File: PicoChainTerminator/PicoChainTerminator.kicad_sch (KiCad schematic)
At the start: 10 parts, among them J1 RJ45, U1 LM78M05_TO252

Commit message: Updated to 1.2
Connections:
- net at R1.1, R2.1: now also J1.6; no longer J1.4
- net at R4.2, R6.1: now also J1.4; no longer J1.6
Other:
- moved on the sheet: R1, R2, R3, R4, R5, R6

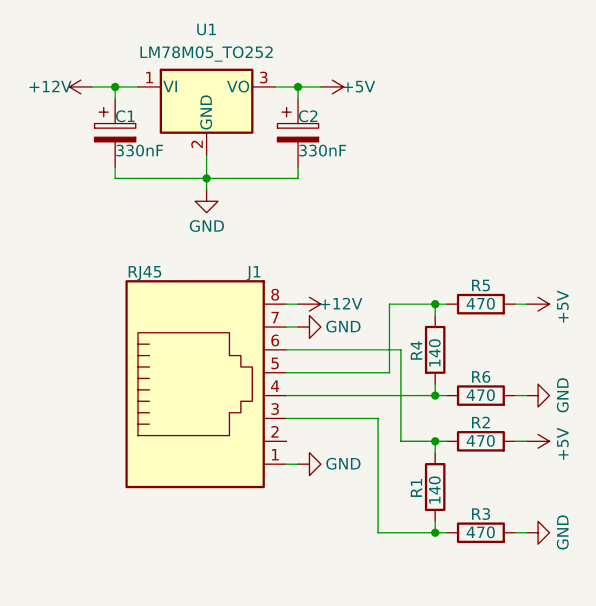
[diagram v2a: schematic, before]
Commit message: Adjusted schematics
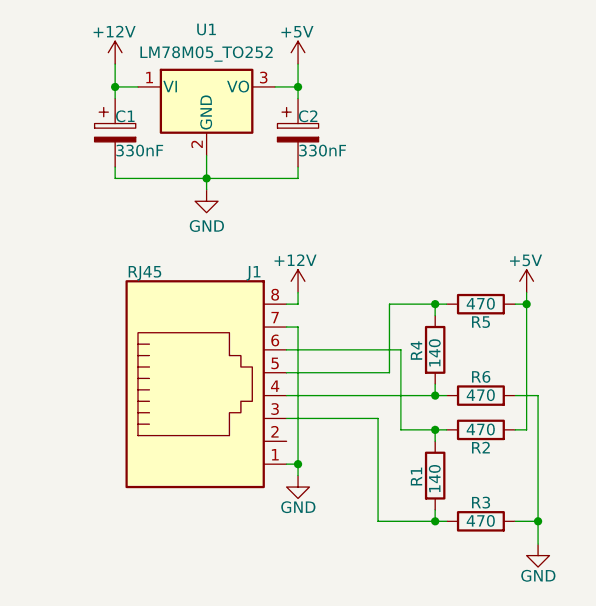
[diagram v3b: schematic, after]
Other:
- moved on the sheet: R1, R2, R3
